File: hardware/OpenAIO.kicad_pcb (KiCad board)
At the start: 8 copper layers, 35 x 35 mm, 341 parts, among them J15 5V, J16 5V, J17 5V, J18 5V, J20 5V, J21 5V, J23 5V, J24 5V, J25 5V, J26 5V, J27 5V, J28 5V, J29 5V, J30 5V, J31 5V, J32 5V, J33 5V, J34 5V, J35 5V, J37 5V, J38 5V, J39 5V, J40 5V, J41 5V, J42 5V, J43 5V, J44 5V, J45 5V, J48 5V, J49 5V, J50 5V, J51 5V, J52 5V, J53 5V, J54 5V, J55 5V, Q1 AP1606, Q10 DOY180N03T, Q11 DOY180N03T, Q12 DOY180N03T, Q13 DOY180N03T, Q14 DOY180N03T, Q15 DOY180N03T, Q16 DOY180N03T, Q17 DOY180N03T, Q18 DOY180N03T, Q19 DOY180N03T, Q2 AP1606, Q20 DOY180N03T, Q21 DOY180N03T, Q22 DOY180N03T, Q23 DOY180N03T, Q24 DOY180N03T, Q25 DOY180N03T, Q26 DOY180N03T, Q3 DOY180N03T, Q4 DOY180N03T, Q5 DOY180N03T, Q6 DOY180N03T, Q7 DOY180N03T, Q8 DOY180N03T, Q9 DOY180N03T, U1 TS2306A 240GF MSM 9_C2976675, U10 COS8051SOT, U11 TLV7031DPWR, U12 SM06B-SRSS-TB(LF)(SN), U13 AT32F421G8U7, U14 NSG2065Q, U15 AT32F421G8U7, U16 NSG2065Q, U17 AT32F421G8U7, U18 NSG2065Q, U19 AT32F421G8U7, U2 RP2354A, U20 NSG2065Q, U21 SX1281IMLTRT, U22 ESP32-C3, U24 AIO_outline, U25 INA186A3IDCKR, U26 BMP580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

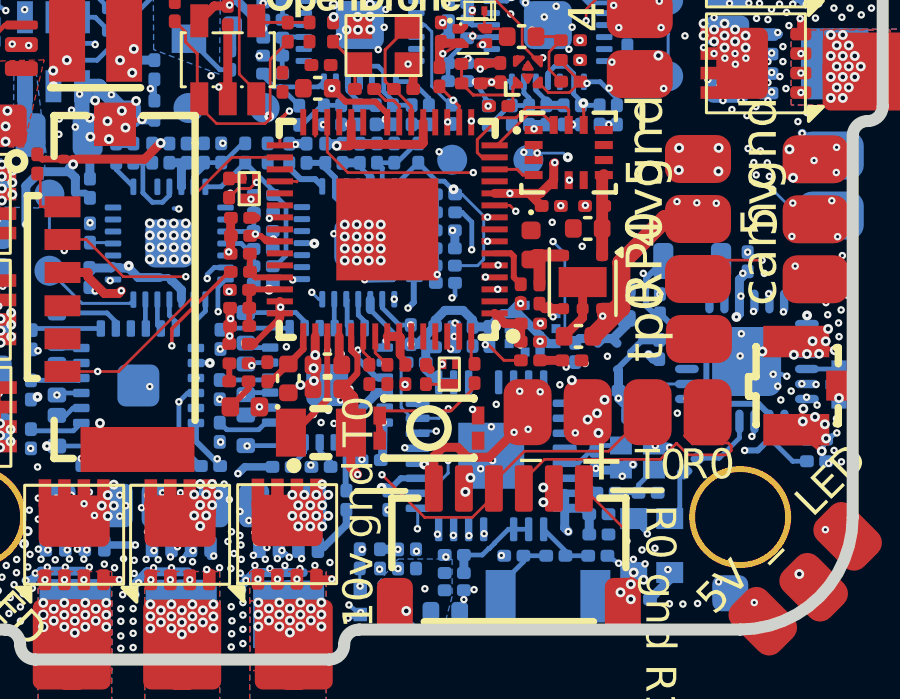
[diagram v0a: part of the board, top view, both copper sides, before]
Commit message: Clean-up: dead track chains, AIO logo to B.Silkscreen, co-located holes ignored
| DRC warning | Before | After |
|---|---|---|
| track_dangling | 7 | 0 (34 dead segments + 1 via, chains) |
| solder_mask_bridge | 109 | 11 (fine-pitch U9/U11, C44/R83, USB1 peg/R4) |
| holes_co_located | 199 | ignored: microvia-on-buried stacks by design |
| Errors / unconnected | 0 / 63 | 0 / 63 |

The "AIO" text was on B.Mask over U26, C82 and vias, exposing copper of
several nets; it is now silkscreen next to "Open".

Co-Authored-By: Claude Opus 5.5 <noreply@anthropic.com>
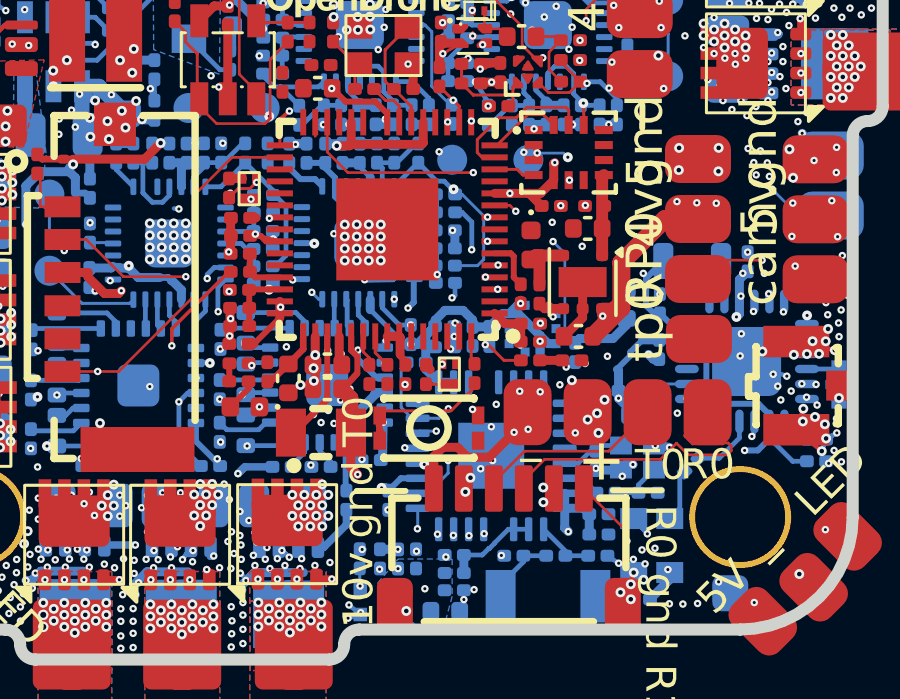
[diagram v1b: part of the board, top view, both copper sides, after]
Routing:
- net USB_D+: track 24.2 -> 12.5 mm
- net UART0_TX: track 17.7 -> 6.55 mm, vias 2 -> 0
- net USB_D-: track 23.6 -> 13.9 mm
- net Net-(Q8-G): track 7.99 -> 0.37 mm
- net +4v5: track 23.0 -> 22.2 mm
- net MOTOR4: track 1.80 -> 1.21 mm

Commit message: Owner: routing in progress
Co-Authored-By: Claude Opus 5.5 <noreply@anthropic.com>
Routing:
- net +5V: track 86.7 -> 57.3 mm
- net +3.3V: track 105.4 -> 84.5 mm
- net BUZZER-: track 20.7 -> 2.38 mm
- net GND: track 148.1 -> 132.0 mm, vias 905 -> 908
- net +10V: track 66.2 -> 50.8 mm
- net /3A: track 1.15 -> 10.4 mm, vias 23 -> 24
- net /Pads/PU0RX: track 11.4 -> 2.52 mm
- net /4A: track 8.47 -> 17.3 mm, vias 22 -> 23
- net +5V_USB: track 21.1 -> 13.1 mm
- net SPI0.MOSI: track 13.7 -> 6.77 mm
- net /4C: track 24.1 -> 18.5 mm
- net +BATT: track 19.8 -> 23.0 mm
- net /Pads/I2C0.SDA: track 18.3 -> 16.1 mm
- net /3B: track 20.8 -> 19.5 mm
- net /3C: track 20.2 -> 19.1 mm
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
